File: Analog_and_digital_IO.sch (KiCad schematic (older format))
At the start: 141 parts, among them J10 22-23-2021, J5 OSTTC020162, J6 22-23-2021, J7 OSTTC030162, J8 22-23-2021, J9 0022232031, Q3 BC817-25LT1G, Q4 BC817-25LT1G, U16 LT1129CST-5#PBF, U17 ISO1211DR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

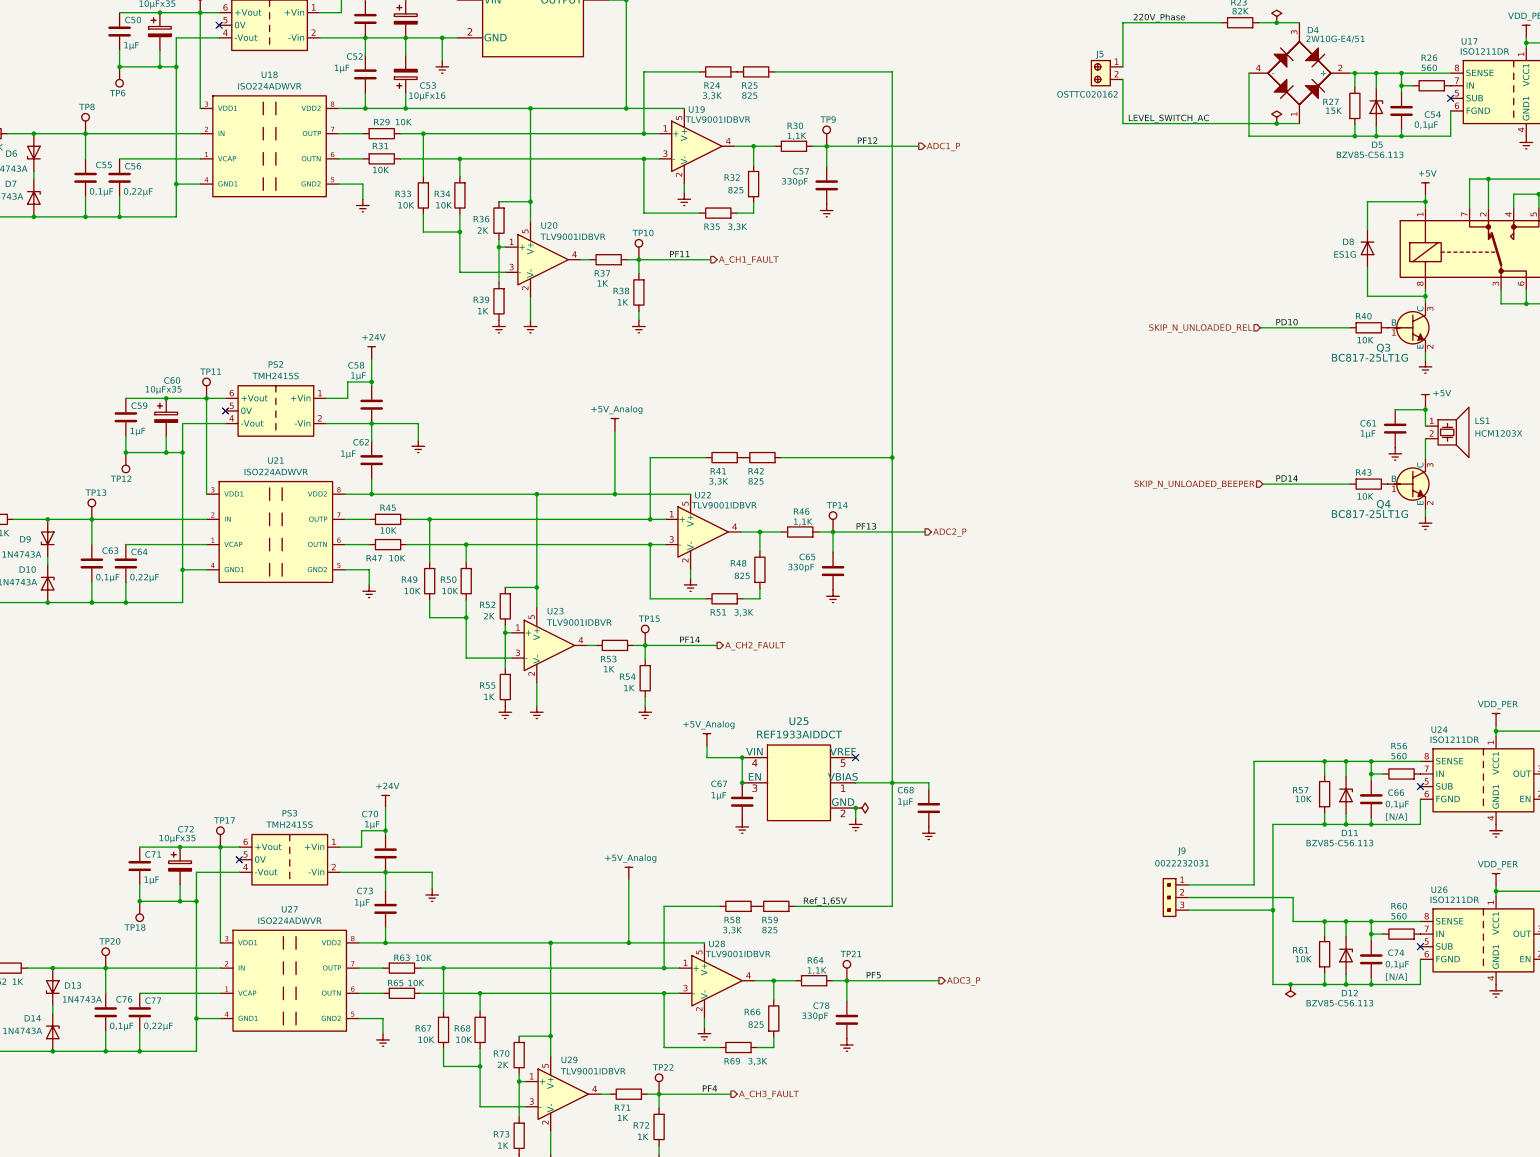
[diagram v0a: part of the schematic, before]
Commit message: corrected few footprints, correct all resistors and capacitors type for ordering
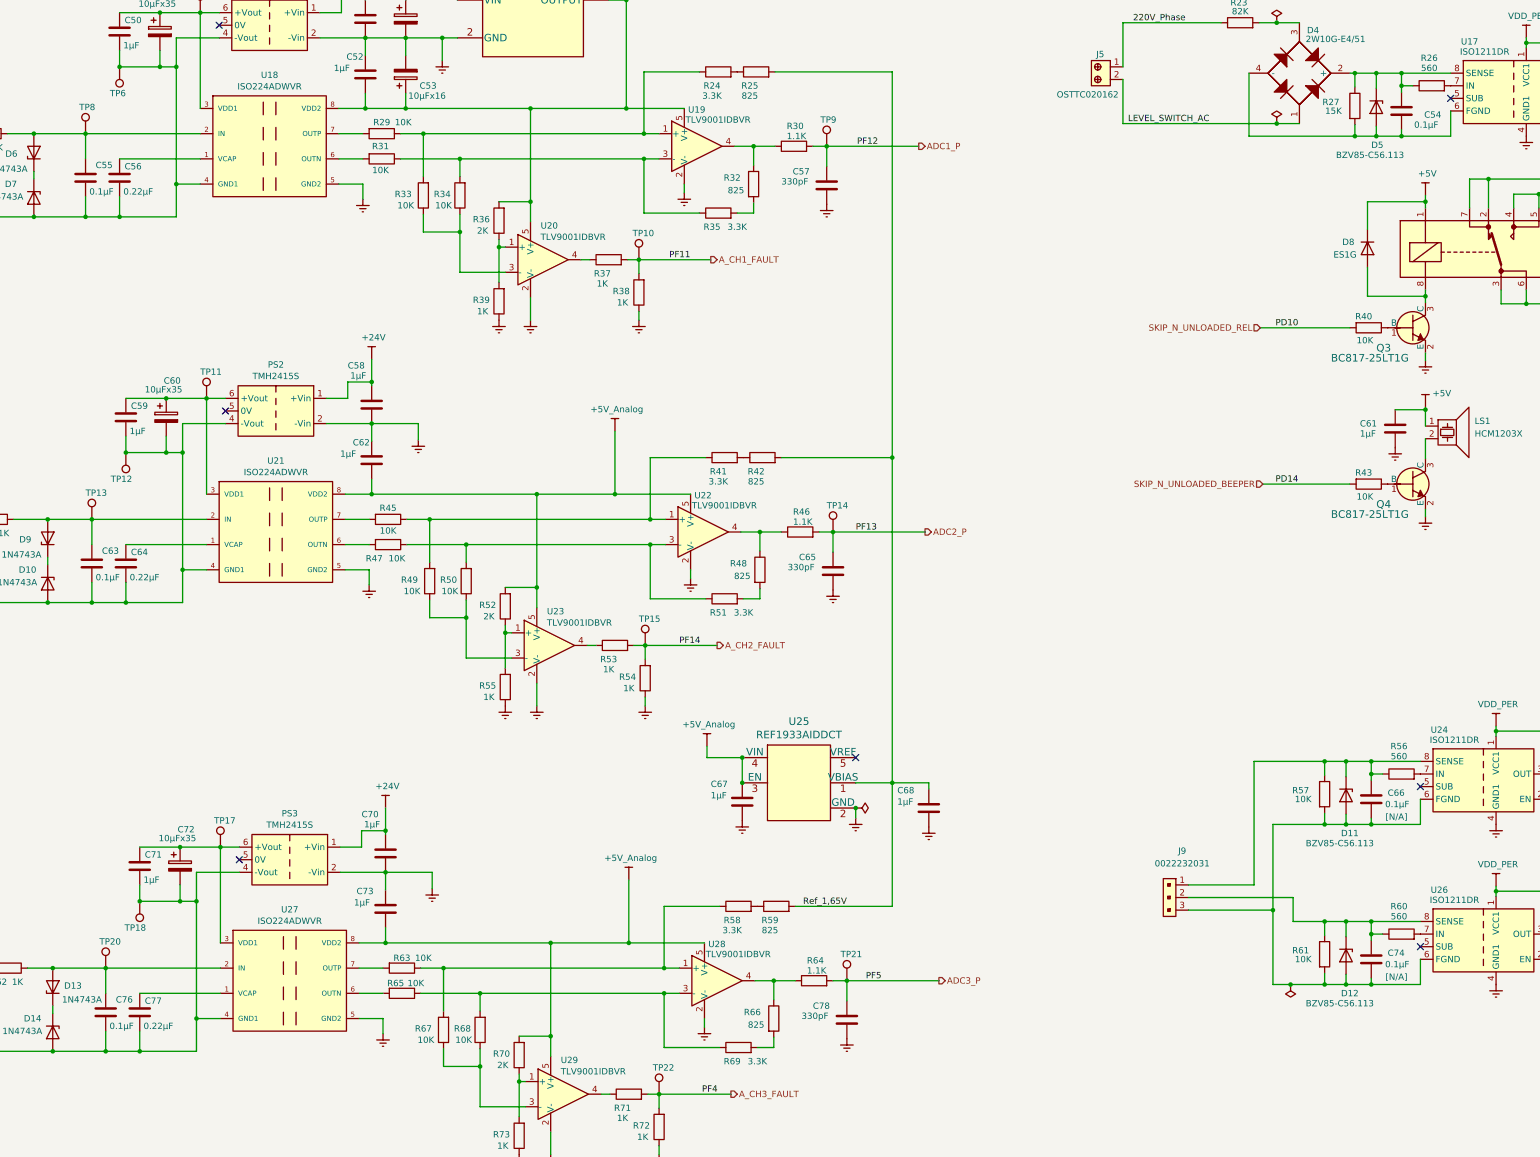
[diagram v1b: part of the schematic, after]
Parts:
- C48, C50, C52, C58, C59, C62, C67, C70, C71, C73: Type CL10B105KA8NNNC -> GRM188R7YA105KA12D
- C54, C66, C74: value 0,1µF -> 0.1µF
- C55, C63, C76: value 0,1µF -> 0.1µF; Type C0603C104K5RACTU -> CL10B104KC8NNNC
- C56, C64, C77: value 0,22µF -> 0.22µF
- C61: Type ?????? CL10B105KA8NNNC -> GRM188R7YA105KA12D
- C65, C78: Type CL10B105KA8NNNC -> GRM188R71H331KA01D
- D4: Type (none) -> 2W10G-E4/51
- L3, L4, L5: Type (none) -> B82790C0225N265
- R24, R35, R41, R51, R58, R69: value 3,3K -> 3.3K; footprint Resistor_SMD:R_0805_2012Metric_Pad1.20x1.40mm_HandSolder -> Resistor_SMD:R_0603_1608Metric_Pad0.98x0.95mm_HandSolder; Type (none) -> RT0603BRD073K3L
- R25, R32, R42, R48, R59, R66: footprint Resistor_SMD:R_0805_2012Metric_Pad1.20x1.40mm_HandSolder -> Resistor_SMD:R_0603_1608Metric_Pad0.98x0.95mm_HandSolder; Type (none) -> RC0603FR-07825RL
- R26, R56, R60: Type (none) -> RC0805FR-07560RL
- R28, R44, R62: Type (none) -> MFR-25FTF52-1K
- R29, R31, R33, R34, R45, R47, R49, R50, R63, R65, R67, R68: Type (none) -> RT0805BRB0710KL
- R30, R46, R64: value 1,1K -> 1.1K; Type (none) -> RC0805FR-071K1L
- R36, R52, R70: Type (none) -> RC0805FR-072KL
- R37, R38, R39, R53, R54, R55, R71, R72, R73: Type (none) -> RC0805FR-071KL
- R40, R43: Type (none) -> RC0805FR-0710KL

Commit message: corrected footprint for B82790C0225N265
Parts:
- L3, L4, L5: footprint Inductor_SMD:L_CommonMode_Delevan_4222 -> SVIELCOM:B82790C0225N265
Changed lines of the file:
@@
 F 0 "L3" H 1740 2501 50  0000 C CNN
 F 1 "B82790C0225N265" H 1550 2420 50  0000 C CNN
-F 2 "Inductor_SMD:L_CommonMode_Delevan_4222" H 1740 2220 50  0001 C CNN
+F 2 "SVIELCOM:B82790C0225N265" H 1740 2220 50  0001 C CNN
 F 3 "https://www.terraelectronica.ru/pdf/show?pdf_file=%252Fds%252Fpdf%252FB%252FB82790.pdf" H 1740 2220 50  0001 C CNN
 F 4 "B82790C0225N265" H 1740 2220 50  0001 C CNN "Type"
@@
 F 0 "L4" H 1790 5561 50  0000 C CNN
 F 1 "B82790C0225N265" H 1600 5480 50  0000 C CNN
-F 2 "Inductor_SMD:L_CommonMode_Delevan_4222" H 1790 5280 50  0001 C CNN
+F 2 "SVIELCOM:B82790C0225N265" H 1790 5280 50  0001 C CNN
 F 3 "https://www.terraelectronica.ru/pdf/show?pdf_file=%252Fds%252Fpdf%252FB%252FB82790.pdf" H 1790 5280 50  0001 C CNN
 F 4 "B82790C0225N265" H 1790 5280 50  0001 C CNN "Type"
@@
 F 0 "L5" H 1900 9121 50  0000 C CNN
 F 1 "B82790C0225N265" H 1710 9040 50  0000 C CNN
-F 2 "Inductor_SMD:L_CommonMode_Delevan_4222" H 1900 8840 50  0001 C CNN
+F 2 "SVIELCOM:B82790C0225N265" H 1900 8840 50  0001 C CNN
 F 3 "https://www.terraelectronica.ru/pdf/show?pdf_file=%252Fds%252Fpdf%252FB%252FB82790.pdf" H 1900 8840 50  0001 C CNN
 F 4 "B82790C0225N265" H 1900 8840 50  0001 C CNN "Type"

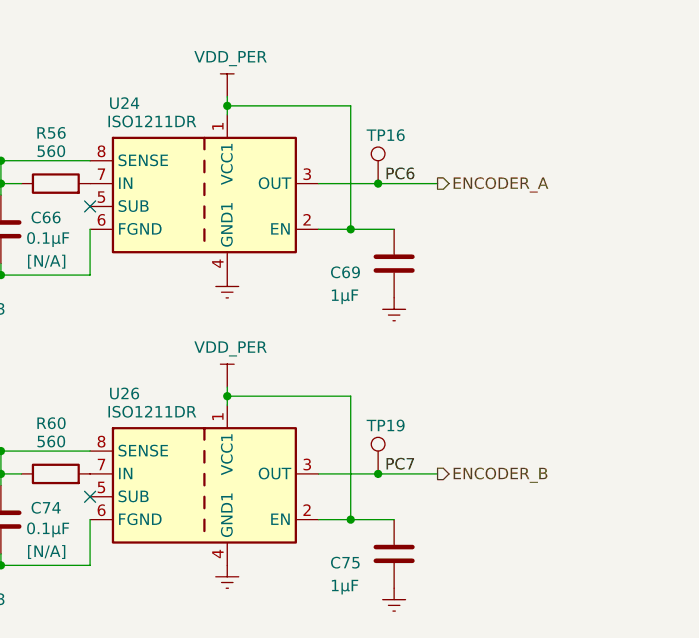
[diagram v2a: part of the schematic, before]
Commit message: deleted TXS0206 added SN74AVCA406DGGR and corrected schema for it
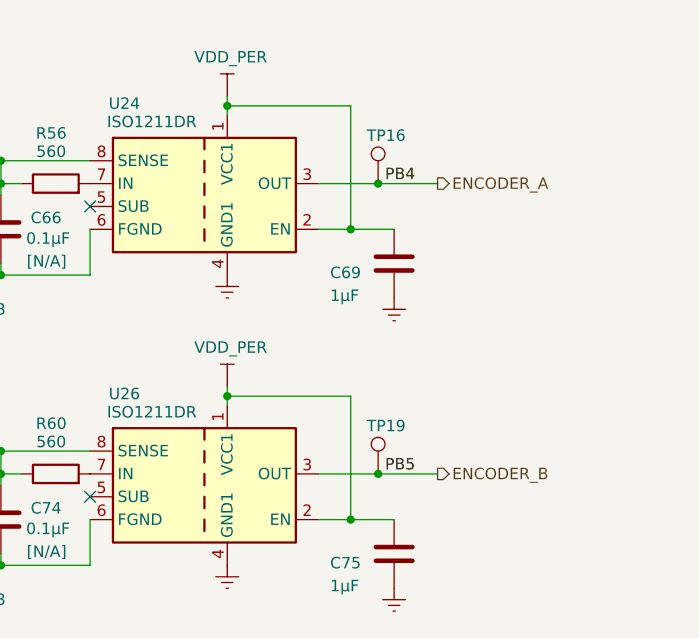
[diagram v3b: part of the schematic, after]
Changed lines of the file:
@@
 ENCODER_A
 Text Label 14810 7200 0    50   ~ 0
-PC6
+PB4
 $Comp
 L Isolator:ISO1211 U?
@@
 ENCODER_B
 Text Label 14810 8470 0    50   ~ 0
-PC7
+PB5
 $Comp
 L dk_Rectangular-Connectors-Headers-Male-Pins:0022232031 J9
